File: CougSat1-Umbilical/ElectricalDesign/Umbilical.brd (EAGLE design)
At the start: 49 x 48 mm, 52 parts, among them J1 USB, J2 Umbilical, J3 5V input, Q1 CSD16406Q3, Q2 CSD16406Q3, U1 FT230XQ, U2 BQ24650

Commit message: Updated Umbilical
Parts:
- added R16, R17: 0Ω <20mΩ, CougsInSpace-Resistors:1608
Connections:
- new net N$1: R16.2, R9.1
- new net N$2: R10.2, R17.1
- net VFB: now also R16.1, R17.2; no longer R10.2, R9.1
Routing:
- net N$2: track 0.00 -> 38.2 mm, vias 0 -> 2
- net N$1: track 0.00 -> 36.2 mm, vias 0 -> 2
- net VFB: track 24.3 -> 43.0 mm, vias 2 -> 5
- net DGND: track 71.9 -> 61.2 mm
- net CHARGING_STAT_G: track 13.3 -> 17.4 mm
- net BTST: track 19.8 -> 18.2 mm
- net UMB_OUT: track 48.7 -> 49.8 mm

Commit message: Updated Umbilical
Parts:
- moved R15 8.74 mm to (1.20, 29.1), turned to 270 degrees
- moved R14 5.37 mm to (20.6, 11.8)
- moved C2 1.30 mm to (11.6, 19.5)
- moved TP5 1.30 mm to (14.7, 19.5)
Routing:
- net UMB_RX: track 48.7 -> 36.5 mm, vias 2 -> 0
- net TXLED_C: track 12.6 -> 3.03 mm
- net CBUS1: track 24.7 -> 16.9 mm
- net CHASSIS: track 22.4 -> 15.9 mm
- net UMB_TX: track 51.3 -> 47.6 mm
- net PGND: track 136.5 -> 134.4 mm
- net !RTS: track 18.6 -> 16.6 mm
- net DIODE_OUT: track 44.0 -> 42.2 mm
- net N$2: track 38.2 -> 36.8 mm
- net UMB_OUT: track 49.8 -> 48.4 mm
- net VFB: track 43.0 -> 44.3 mm
- net USB_RESET: track 12.8 -> 11.6 mm
- net USB_CONN_N: track 7.58 -> 8.86 mm

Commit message: Updated Umbilical
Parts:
- moved R1 9.22 mm to (19.0, 29.1), turned to 270 degrees
- moved C6 2.33 mm to (15.1, 28.1)
- moved TP6 0.60 mm to (18.3, 25.7)
- moved TP3 0.10 mm to (37.3, 19.8)
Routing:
- net CHASSIS: track 15.9 -> 31.6 mm
- net PGND: track 134.4 -> 123.7 mm
- net DGND: track 61.2 -> 54.4 mm
- net USB5V_FILTERED: track 16.2 -> 12.5 mm
- net 3.3V: track 50.0 -> 46.7 mm
- net 5.0V: track 44.5 -> 42.3 mm
- net UMB_TX: track 47.6 -> 45.4 mm
- net DIODE_OUT: track 42.2 -> 40.4 mm
- net N$1: track 36.2 -> 34.7 mm
- net CBUS2: track 9.91 -> 8.62 mm
- net UMB_OUT: track 48.4 -> 47.6 mm
- net CHARGING_STAT_R: track 3.71 -> 3.17 mm

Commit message: Updated Umbilical
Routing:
- net CHASSIS: track 31.6 -> 15.9 mm
- net TS: track 10.5 -> 9.34 mm
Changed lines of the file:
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@@
 <via x="34.088709375" y="27.8267375" extent="1-16" drill="0.35"/>
 <via x="32.3" y="23.70499375" extent="1-16" drill="0.35"/>
-<wire x1="31.9" y1="20.9" x2="33.6" y2="22.6" width="0.38" layer="1"/>
-<wire x1="33.6" y1="22.6" x2="33.6" y2="23.935" width="0.38" layer="1"/>
+<wire x1="31.9" y1="20.9" x2="33.6" y2="22.6" width="0.2" layer="1"/>
+<wire x1="33.6" y1="22.6" x2="33.6" y2="23.935" width="0.2" layer="1"/>
 <wire x1="33.6" y1="23.935" x2="33.36999375" y2="23.70499375" width="0.38" layer="1"/>
-<wire x1="33.36999375" y1="23.70499375" x2="32.3" y2="23.70499375" width="0.38" layer="1"/>
-<wire x1="34.088709375" y1="27.8267375" x2="31.642421875" y2="25.38045" width="0.38" layer="16"/>
-<wire x1="33.665446875" y1="28.25" x2="32.05" y2="28.25" width="0.38" layer="1"/>
-<wire x1="31.85" y1="28.05" x2="32.05" y2="28.25" width="0.38" layer="1"/>
-<wire x1="33.665446875" y1="28.25" x2="34.088709375" y2="27.8267375" width="0.38" layer="1"/>
-<wire x1="28.93" y1="24.647525" x2="28.93" y2="24.092475" width="0.37" layer="16"/>
-<wire x1="28.93" y1="24.092475" x2="29.322475" y2="23.7" width="0.37" layer="16"/>
-<wire x1="29.322475" y1="23.7" x2="29.877525" y2="23.7" width="0.37" layer="16"/>
+<wire x1="33.36999375" y1="23.70499375" x2="32.3" y2="23.70499375" width="0.2" layer="1"/>
+<wire x1="34.088709375" y1="27.8267375" x2="31.642421875" y2="25.38045" width="0.2" layer="16"/>
+<wire x1="33.665446875" y1="28.25" x2="32.05" y2="28.25" width="0.2" layer="1"/>
+<wire x1="31.85" y1="28.05" x2="32.05" y2="28.25" width="0.2" layer="1"/>
+<wire x1="33.665446875" y1="28.25" x2="34.088709375" y2="27.8267375" width="0.2" layer="1"/>
+<wire x1="28.93" y1="24.647525" x2="28.93" y2="24.092475" width="0.2" layer="16"/>
+<wire x1="28.93" y1="24.092475" x2="29.322475" y2="23.7" width="0.2" layer="16"/>
+<wire x1="29.322475" y1="23.7" x2="29.877525" y2="23.7" width="0.2" layer="16"/>
 <wire x1="31.642421875" y1="25.38045" x2="31.637415625" y2="25.37544375" width="0.37" layer="16"/>
-<wire x1="29.877525" y1="23.7" x2="29.88251875" y2="23.70499375" width="0.37" layer="16"/>
-<wire x1="29.88251875" y1="23.70499375" x2="32.3" y2="23.70499375" width="0.37" layer="16"/>
-<wire x1="31.637415625" y1="25.37544375" x2="29.65791875" y2="25.37544375" width="0.37" layer="16"/>
-<wire x1="29.65791875" y1="25.37544375" x2="28.93" y2="24.647525" width="0.37" layer="16"/>
+<wire x1="29.877525" y1="23.7" x2="29.88251875" y2="23.70499375" width="0.2" layer="16"/>
+<wire x1="29.88251875" y1="23.70499375" x2="32.3" y2="23.70499375" width="0.2" layer="16"/>
+<wire x1="31.637415625" y1="25.37544375" x2="29.65791875" y2="25.37544375" width="0.2" layer="16"/>
+<wire x1="29.65791875" y1="25.37544375" x2="28.93" y2="24.647525" width="0.2" layer="16"/>
 </signal>
 <signal name="5.0V">
@@
 <contactref element="R4" pad="1"/>
 <wire x1="30.935" y1="32.6" x2="31.205" y2="32.33" width="0.355" layer="1"/>
-<wire x1="31.205" y1="32.33" x2="31.205" y2="30.79" width="0.355" layer="1"/>
+<wire x1="31.205" y1="32.33" x2="31.205" y2="30.79" width="0.2" layer="1"/>
 <wire x1="30.85" y1="30.435" x2="31.205" y2="30.79" width="0.37" layer="1"/>
-<wire x1="30.85" y1="29.05" x2="30.85" y2="30.435" width="0.3" layer="1"/>
+<wire x1="30.85" y1="29.05" x2="30.85" y2="30.435" width="0.2" layer="1"/>
 </signal>
 <signal name="PH">
@@
 <contactref element="R12" pad="2"/>
 <contactref element="U2" pad="4"/>
-<wire x1="24.1" y1="28.965" x2="26" y2="28.965" width="0.16" layer="1"/>
+<wire x1="24.1" y1="28.965" x2="25.3" y2="28.965" width="0.2" layer="1"/>
+<wire x1="25.3" y1="28.965" x2="26" y2="28.965" width="0.16" layer="1"/>
 <wire x1="26" y1="28.965" x2="29.3" y2="28.965" width="0.16" layer="1"/>
 <wire x1="29.3" y1="28.965" x2="29.35" y2="28.965" width="0.16" layer="1"/>
 <wire x1="29.35" y1="28.965" x2="29.35" y2="29.05" width="0.16" layer="1"/>
-<wire x1="24.1" y1="28.965" x2="29.3" y2="28.965" width="0.38" layer="1"/>
+<wire x1="25.3" y1="28.965" x2="29.3" y2="28.965" width="0.2" layer="1"/>
 </signal>
 <signal name="UMB_OUT">
@@
 <wire x1="16.82" y1="11.1" x2="16.8" y2="11.1" width="0.355" layer="1"/>
 <contactref element="R14" pad="1"/>
-<wire x1="16.82" y1="11.1" x2="16.9" y2="11.1" width="0.35" layer="1"/>
-<wire x1="16.9" y1="11.1" x2="20.435" y2="11.1" width="0.35" layer="1"/>
 <wire x1="20.435" y1="11.1" x2="20.6" y2="10.935" width="0.35" layer="1"/>
-<wire x1="4.78" y1="11.1" x2="16.9" y2="11.1" width="0.4" layer="1"/>
 <wire x1="16.82" y1="11.1" x2="20.435" y2="11.1" width="0.4" layer="1"/>
 </signal>
@@
 <contactref element="RN1" pad="3"/>
 <via x="6.9" y="40.4" extent="1-16" drill="0.35"/>
-<wire x1="6.9" y1="40.4" x2="6.9" y2="36.5" width="0.3" layer="16"/>
-<wire x1="8.7" y1="34.7" x2="8.7" y2="34.4" width="0.3" layer="16"/>
+<wire x1="6.9" y1="40.4" x2="6.9" y2="36.5" width="0.2" layer="16"/>
+<wire x1="8.7" y1="34.7" x2="8.7" y2="34.4" width="0.2" layer="16"/>
 <via x="8.7" y="34.4" extent="1-16" drill="0.35"/>
-<wire x1="6.9" y1="36.5" x2="8.7" y2="34.7" width="0.3" layer="16"/>
-<wire x1="9.73" y1="41.37840625" x2="9.34840625" y2="41.76" width="0.3" layer="1"/>
+<wire x1="6.9" y1="36.5" x2="8.7" y2="34.7" width="0.2" layer="16"/>
+<wire x1="9.73" y1="41.37840625" x2="9.34840625" y2="41.76" width="0.2" layer="1"/>
 <wire x1="9.73" y1="41.37840625" x2="9.73" y2="41.13" width="0.3" layer="1"/>
 <wire x1="9.7" y1="41.1" x2="9.73" y2="41.13" width="0.3" layer="1"/>
-<wire x1="9.34840625" y1="41.76" x2="8.26" y2="41.76" width="0.3" layer="1"/>
-<wire x1="8.26" y1="41.76" x2="6.9" y2="40.4" width="0.3" layer="1"/>
-<wire x1="8.7" y1="31.50340625" x2="8.7" y2="34.4" width="0.3" layer="1"/>
+<wire x1="9.34840625" y1="41.76" x2="8.26" y2="41.76" width="0.2" layer="1"/>
+<wire x1="8.26" y1="41.76" x2="6.9" y2="40.4" width="0.2" layer="1"/>
+<wire x1="8.7" y1="31.50340625" x2="8.7" y2="34.4" width="0.2" layer="1"/>
 <wire x1="7.025" y1="29.1" x2="7.025" y2="29.82840625" width="0.3" layer="1"/>
-<wire x1="7.025" y1="29.82840625" x2="8.7" y2="31.50340625" width="0.3" layer="1"/>
+<wire x1="7.025" y1="29.82840625" x2="8.7" y2="31.50340625" width="0.2" layer="1"/>
 </signal>
 <signal name="N$1">

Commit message: Updated Umbilical
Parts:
- moved R17 26.9 mm to (42.4, 36.1), turned to 0 degrees
- moved R16 26.7 mm to (45.5, 36.1)
- moved TP3 9.74 mm to (36.4, 10.1)
- moved TP4 8.94 mm to (47.4, 31.6)
- moved J2 8.94 mm to (42.6, 41.0), turned to 0 degrees
- moved RN1 8.86 mm to (7.60, 31.9)
- moved R14 8.86 mm to (21.6, 20.6)
- moved C16 8.44 mm to (38.2, 27.5), turned to 90 degrees
- moved R10 7.79 mm to (42.4, 34.3), turned to 180 degrees
- moved D1 7.53 mm to (45.3, 11.5)
- moved C9 7.07 mm to (45.6, 15.8)
- moved J3 7.01 mm to (42.6, 4.60)
- moved L1 6.82 mm to (40.0, 22.3)
- moved Q1 6.76 mm to (37.8, 16.4)
- moved TP1 6.76 mm to (40.2, 10.1)
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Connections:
- net N$1 renamed FEEDBACK_HIGH
- net N$2 renamed FEEDBACK_LOW
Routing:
- net FEEDBACK_LOW: track 36.6 -> 1.80 mm, vias 2 -> 0
- net FEEDBACK_HIGH: track 34.7 -> 10.1 mm
- net PGND: track 123.7 -> 103.6 mm, vias 4 -> 7
- net VFB: track 44.1 -> 26.0 mm, vias 5 -> 2
- net CHASSIS: track 15.9 -> 33.9 mm
- net PH: track 23.6 -> 38.4 mm, vias 2 -> 8
- net 3.3V: track 46.7 -> 34.5 mm
- net CHARGING_STAT_G: track 17.4 -> 6.13 mm, vias 2 -> 0
- net HIGHDV: track 12.1 -> 22.9 mm, vias 0 -> 2
- net !CTS: track 20.2 -> 10.4 mm, vias 4 -> 2
- net CHARGING_STAT_R: track 3.17 -> 12.4 mm, vias 0 -> 2
- net UMB_TX: track 45.4 -> 54.4 mm, vias 6 -> 2
- net !RTS: track 16.6 -> 7.89 mm
- net UMB_RX: track 36.1 -> 44.3 mm, vias 0 -> 2
- net SR_P: track 24.1 -> 16.2 mm
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
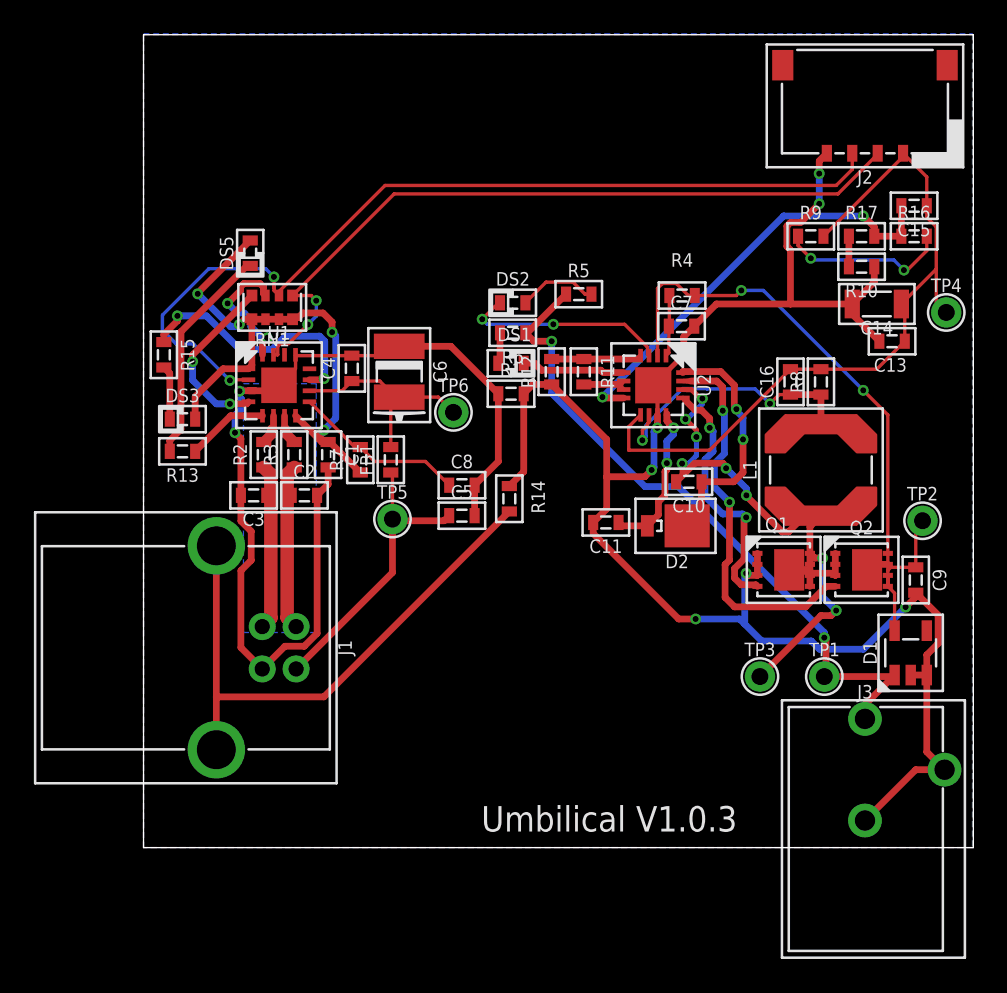
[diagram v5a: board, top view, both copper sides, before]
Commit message: Fixed trace width issues
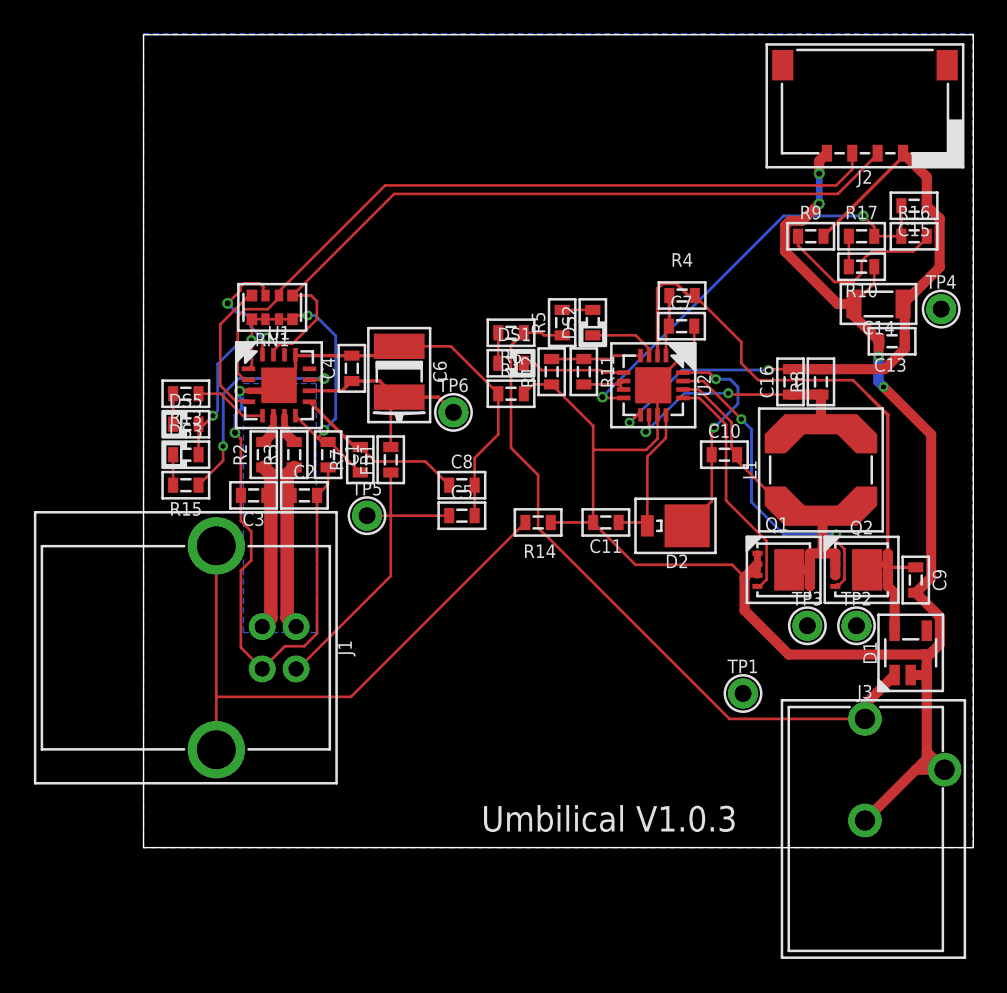
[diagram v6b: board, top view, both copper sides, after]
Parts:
- moved DS5 10.8 mm to (2.50, 25.0), turned to 0 degrees
- moved R15 7.81 mm to (2.50, 21.4), turned to 180 degrees
- moved TP2 7.32 mm to (42.1, 13.1)
- moved TP1 4.90 mm to (35.4, 9.10)
- moved DS2 4.87 mm to (26.5, 31.0), turned to 90 degrees
- moved TP3 4.10 mm to (39.2, 13.1)
- moved R13 3.41 mm to (2.50, 26.8)
- moved C10 2.64 mm to (34.3, 23.2), turned to 0 degrees
- moved R14 2.20 mm to (23.3, 19.2), turned to 0 degrees
- moved DS3 2.11 mm to (2.50, 23.2)
- moved R5 1.94 mm to (24.7, 31.0), turned to 90 degrees
- moved TP5 1.51 mm to (13.2, 19.6)
- moved TP4 0.36 mm to (47.1, 31.8)
- moved C14 0.10 mm to (43.4, 32.1)
- moved R6 0.10 mm to (21.7, 30.4)
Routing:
- net PH: track 38.4 -> 21.6 mm, vias 8 -> 0
- net RXLED_C: track 13.0 -> 1.80 mm
- net UMB_TX: track 54.4 -> 45.2 mm, vias 2 -> 0
- net CHARGING_STAT_R: track 12.4 -> 4.06 mm, vias 2 -> 0
- net 3.3V: track 34.5 -> 29.1 mm
- net UMB_OUT: track 43.8 -> 39.2 mm, vias 0 -> 2
- net HIGHDV: track 22.9 -> 18.9 mm
- net PGND: track 103.6 -> 106.9 mm, vias 7 -> 4
- net CHARGING_STAT_R_LED: track 4.70 -> 1.81 mm
- net !CTS: track 10.4 -> 8.25 mm, vias 2 -> 0
- net 5.0V: track 40.3 -> 42.4 mm, vias 2 -> 0
- net SR_P: track 16.2 -> 14.2 mm
- net DIODE_OUT: track 41.0 -> 39.2 mm, vias 2 -> 0
- net CBUS1: track 15.0 -> 13.2 mm
- net TXLED_C: track 3.19 -> 1.80 mm
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
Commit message: Updated Umbilical
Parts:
- moved TP2 0.40 mm to (41.7, 13.1)
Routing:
- net PH: track 21.6 -> 25.6 mm
- net DIODE_OUT: track 39.2 -> 42.9 mm
- net UMB_OUT: track 39.2 -> 41.6 mm
- net 5.0V: track 42.4 -> 43.8 mm
- removed copper zone on layer 1, net BALANCING-TOP
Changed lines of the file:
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@@
 <attribute name="NAME" x="35.4" y="10.7" size="0.8" layer="25" font="vector" ratio="15" align="center"/>
 </element>
-<element name="TP2" library="CougsInSpace-Connectors" package="THT-1.0" value="TEST_POINT-THT-1.0" x="42.1" y="13.1" smashed="yes">
-<attribute name="NAME" x="42.1" y="14.7" size="0.8" layer="25" font="vector" ratio="15" align="center"/>
+<element name="TP2" library="CougsInSpace-Connectors" package="THT-1.0" value="TEST_POINT-THT-1.0" x="41.7" y="13.1" smashed="yes">
+<attribute name="NAME" x="41.7" y="14.7" size="0.8" layer="25" font="vector" ratio="15" align="center"/>
 </element>
 <element name="TP3" library="CougsInSpace-Connectors" package="THT-1.0" value="TEST_POINT-THT-1.0" x="39.2" y="13.1" smashed="yes">
@@
 <wire x1="35.3" y1="28.6" x2="36.3" y2="27.6" width="0.16" layer="1"/>
 <wire x1="36.3" y1="27.6" x2="41.9" y2="27.6" width="0.16" layer="1"/>
-<wire x1="42.1" y1="13.1" x2="44.35" y2="12.81" width="0" layer="19" extent="1-1"/>
+<wire x1="42.725" y1="16.4" x2="42.725" y2="14.125" width="0.16" layer="1"/>
+<wire x1="42.725" y1="14.125" x2="41.7" y2="13.1" width="0.16" layer="1"/>
 </signal>
 <signal name="BTST">
@@
 <contactref element="J3" pad="1"/>
 <contactref element="TP1" pad="1"/>
-<wire x1="44.35" y1="10.19" x2="44.26" y2="10.1" width="0.4" layer="1"/>
-<wire x1="22.57" y1="30.4" x2="22.45" y2="30.4" width="0.16" layer="1"/>
 <wire x1="42.6" y1="7.6" x2="42.6" y2="8.44" width="0.6" layer="1"/>
 <wire x1="42.6" y1="8.44" x2="44.35" y2="10.19" width="0.6" layer="1"/>
@@
 <wire x1="23.5" y1="30.4" x2="23.65" y2="30.25" width="0.16" layer="1"/>
 <wire x1="22.45" y1="30.4" x2="23.5" y2="30.4" width="0.16" layer="1"/>
-<wire x1="42.6" y1="7.6" x2="34.6" y2="7.6" width="0.16" layer="1"/>
+<wire x1="42.6" y1="7.6" x2="35.8" y2="7.6" width="0.16" layer="1"/>
+<wire x1="35.8" y1="7.6" x2="34.6" y2="7.6" width="0.16" layer="1"/>
 <wire x1="23.69" y1="18.51" x2="23.6505875" y2="18.51" width="0.16" layer="1"/>
 <wire x1="23.6505875" y1="18.51" x2="23.3" y2="18.8605875" width="0.16" layer="1"/>
@@
 <wire x1="23.3" y1="22" x2="21.7" y2="23.6" width="0.16" layer="1"/>
 <wire x1="21.7" y1="23.6" x2="21.7" y2="29.65" width="0.16" layer="1"/>
-<wire x1="42.6" y1="7.6" x2="35.4" y2="9.1" width="0" layer="19" extent="1-1"/>
+<wire x1="35.8" y1="7.6" x2="35.4" y2="8" width="0.16" layer="1"/>
+<wire x1="35.4" y1="8" x2="35.4" y2="9.1" width="0.16" layer="1"/>
 </signal>
 <signal name="CHARGING_STAT_G">
@@
 <contactref element="TP3" pad="1"/>
 <wire x1="40" y1="19.6" x2="39.0401875" y2="19.6" width="0.4" layer="1"/>
-<wire x1="40.85" y1="17.375" x2="40.85" y2="16.075" width="0.6" layer="1"/>
-<wire x1="39.35" y1="17.375" x2="39.35" y2="16.4" width="0.6" layer="1"/>
-<wire x1="39.35" y1="16.4" x2="39.35" y2="15.425" width="0.6" layer="1"/>
+<wire x1="40.85" y1="17.375" x2="40.85" y2="16.6" width="0.6" layer="1"/>
+<wire x1="40.85" y1="16.6" x2="40.85" y2="16.075" width="0.6" layer="1"/>
+<wire x1="39.35" y1="17.375" x2="39.35" y2="16.8" width="0.6" layer="1"/>
+<wire x1="39.35" y1="16.8" x2="39.35" y2="16.4" width="0.6" layer="1"/>
+<wire x1="39.35" y1="15.425" x2="39.35" y2="16" width="0.6" layer="1"/>
+<wire x1="39.35" y1="16" x2="39.35" y2="16.4" width="0.6" layer="1"/>
 <wire x1="38.125" y1="16.4" x2="39.35" y2="16.4" width="0.6" layer="1"/>
 <wire x1="40.85" y1="17.375" x2="40.1" y2="17.375" width="0.6" layer="1"/>
@@
 <wire x1="34.72" y1="23.53" x2="34.72" y2="25.11631875" width="0.16" layer="1"/>
 <wire x1="34.72" y1="25.11631875" x2="32.78631875" y2="27.05" width="0.16" layer="1"/>
-<wire x1="40.85" y1="16.075" x2="40.85" y2="16.725" width="0" layer="19" extent="1-1"/>
-<wire x1="39.35" y1="16.075" x2="39.35" y2="15.425" width="0" layer="19" extent="1-1"/>
-<wire x1="39.35" y1="16.725" x2="39.35" y2="17.375" width="0" layer="19" extent="1-1"/>
-<wire x1="39.2" y1="13.1" x2="39.35" y2="15.425" width="0" layer="19" extent="1-1"/>
+<wire x1="38.125" y1="16.4" x2="39.2" y2="15.325" width="0.16" layer="1"/>
+<wire x1="39.2" y1="15.325" x2="39.2" y2="13.1" width="0.16" layer="1"/>
+<wire x1="40.85" y1="16.725" x2="40.85" y2="16.6" width="0.16" layer="1"/>
+<wire x1="39.35" y1="16.725" x2="39.35" y2="16.8" width="0.16" layer="1"/>
+<wire x1="39.35" y1="16.075" x2="39.35" y2="16" width="0.16" layer="1"/>
 </signal>
 <signal name="HIGHDV">
@@
 <wire x1="36.9" y1="28.2" x2="36.95" y2="28.25" width="0.16" layer="1"/>
 <wire x1="36.95" y1="28.25" x2="38.2" y2="28.25" width="0.16" layer="1"/>
-<wire x1="44.85" y1="32.1" x2="47.1" y2="31.8" width="0" layer="19" extent="1-1"/>
+<wire x1="44.85" y1="32.1" x2="46.8" y2="32.1" width="0.16" layer="1"/>
+<wire x1="46.8" y1="32.1" x2="47.1" y2="31.8" width="0.16" layer="1"/>
 </signal>
 <signal name="UMB_RX">
@@
 <wire x1="10.2875" y1="24.1875" x2="10.525" y2="23.95" width="0.16" layer="1"/>
 <wire x1="10.525" y1="23.95" x2="10.9" y2="23.95" width="0.16" layer="1"/>
-<wire x1="6.4" y1="31.2" x2="6.4" y2="28.475" width="0.16" layer="1"/>
+<wire x1="6.4" y1="28.475" x2="6.4" y2="30.2" width="0.16" layer="1"/>
+<wire x1="6.4" y1="30.2" x2="6.4" y2="31.2" width="0.16" layer="1"/>
 <wire x1="6.4" y1="28.475" x2="6.2" y2="28.275" width="0.16" layer="1"/>
 <wire x1="12.8" y1="22.15" x2="11" y2="23.95" width="0.16" layer="1"/>
@@
 <wire x1="9.025" y1="31.425" x2="8.8" y2="31.2" width="0.16" layer="1"/>
 <wire x1="11.35" y1="30.2187375" x2="10.1437375" y2="31.425" width="0.16" layer="16"/>
-<wire x1="6.4" y1="30.1" x2="6.4" y2="31.2" width="0" layer="19" extent="1-1"/>
+<wire x1="6.365" y1="29.97131875" x2="6.365" y2="30.165" width="0.16" layer="1"/>
+<wire x1="6.365" y1="30.165" x2="6.4" y2="30.2" width="0.16" layer="1"/>
 </signal>
 <signal name="DGND">
@@
 </signal>
 <signal name="BALANCING-TOP">
-<polygon width="0.16" layer="1" spacing="0.5" pour="hatch" rank="6">
-<vertex x="0" y="0"/>
-<vertex x="0" y="48"/>
-<vertex x="49" y="48"/>
-<vertex x="49" y="0"/>
-</polygon>
 </signal>
 <signal name="CBUS1">

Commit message: Update umbilical
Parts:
- moved TP5 4.94 mm to (17.2, 16.7)
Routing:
- net USB5V: track 18.8 -> 20.0 mm
- net 3.3V: track 29.4 -> 30.2 mm
- net UMB_TX: track 45.2 -> 45.9 mm
- net USB5V_FILTERED: track 12.6 -> 11.9 mm
